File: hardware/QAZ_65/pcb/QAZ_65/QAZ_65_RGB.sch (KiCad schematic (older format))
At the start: 45 parts, among them U3 IS31FL3746A

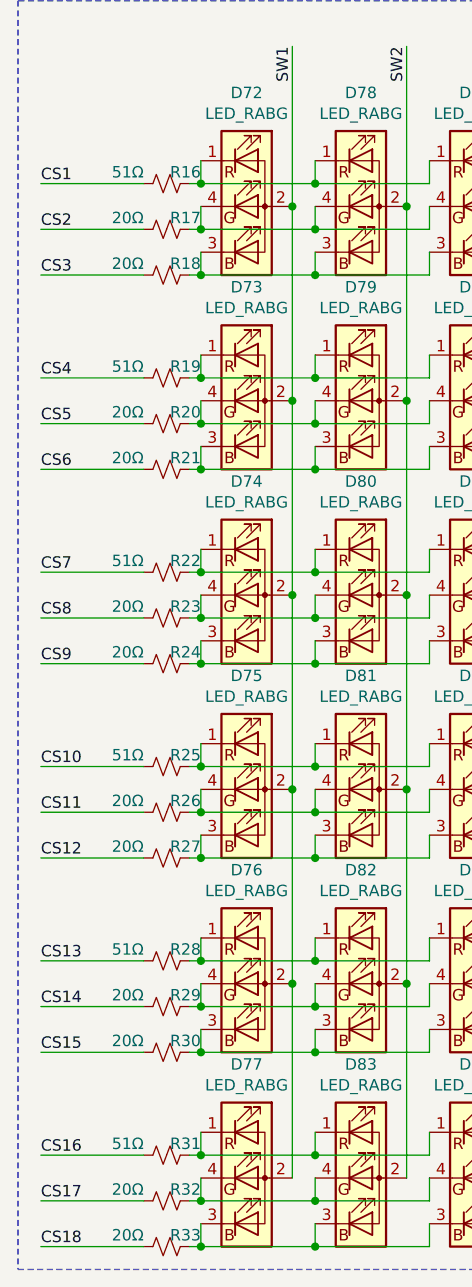
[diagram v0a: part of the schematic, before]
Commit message: layers: added v2/v3 layers for qaz 65%
closes #4

v2 has slightly altered holes on the top of the outline, since the SWD
connector is not brought out.

v3 is for using a pcb as the plate layer (not sure if it will work..)
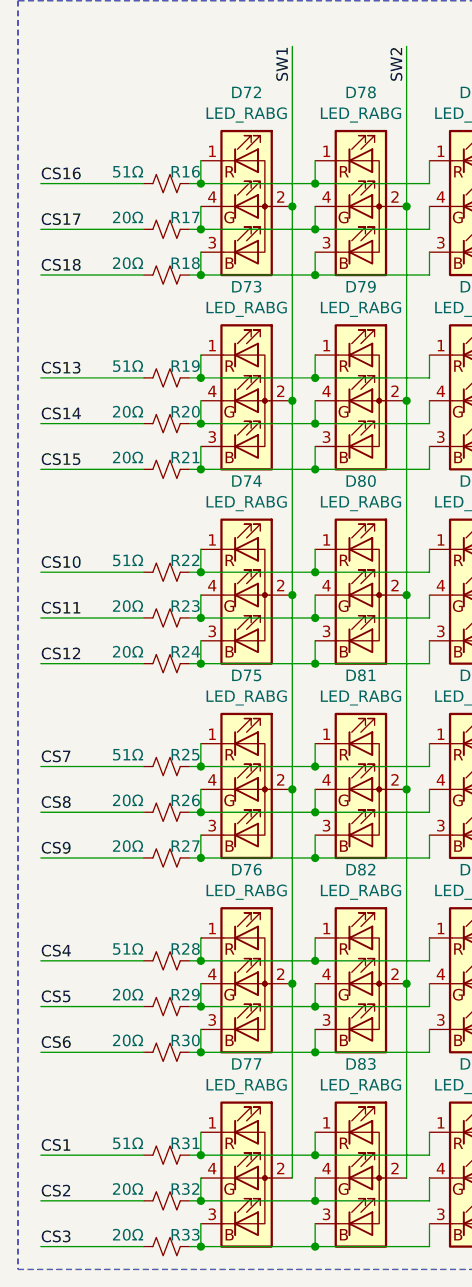
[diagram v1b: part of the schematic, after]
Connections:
- net CS1: now also R31.2; no longer R16.2
- net CS10: now also R22.2; no longer R25.2
- net CS11: now also R23.2; no longer R26.2
- net CS12: now also R24.2; no longer R27.2
- net CS13: now also R19.2; no longer R28.2
- net CS14: now also R20.2; no longer R29.2
- net CS15: now also R21.2; no longer R30.2
- net CS16: now also R16.2; no longer R31.2
- net CS17: now also R17.2; no longer R32.2
- net CS18: now also R18.2; no longer R33.2
- net CS2: now also R32.2; no longer R17.2
- net CS3: now also R33.2; no longer R18.2
- net CS4: now also R28.2; no longer R19.2
- net CS5: now also R29.2; no longer R20.2
- net CS6: now also R30.2; no longer R21.2
- net CS7: now also R25.2; no longer R22.2
- net CS8: now also R26.2; no longer R23.2
- net CS9: now also R27.2; no longer R24.2
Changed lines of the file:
@@
 Wire Wire Line
 	2950 2550 2900 2550
-Text Label 2250 2550 0    50   ~ 0
+Text Label 2250 6800 0    50   ~ 0
 CS3
 Wire Wire Line
-	2700 2550 2250 2550
-Text Label 2250 2350 0    50   ~ 0
+	2700 6800 2250 6800
+Text Label 2250 6600 0    50   ~ 0
 CS2
 Wire Wire Line
-	2700 2350 2250 2350
-Text Label 2250 2150 0    50   ~ 0
+	2700 6600 2250 6600
+Text Label 2250 6400 0    50   ~ 0
 CS1
 Wire Wire Line
-	2700 2150 2250 2150
+	2700 6400 2250 6400
 Wire Wire Line
 	2950 2050 2950 2150
@@
 Wire Wire Line
 	2950 3400 2900 3400
-Text Label 2250 3400 0    50   ~ 0
+Text Label 2250 5950 0    50   ~ 0
 CS6
 Wire Wire Line
-	2700 3400 2250 3400
-Text Label 2250 3200 0    50   ~ 0
+	2700 5950 2250 5950
+Text Label 2250 5750 0    50   ~ 0
 CS5
 Wire Wire Line
-	2700 3200 2250 3200
-Text Label 2250 3000 0    50   ~ 0
+	2700 5750 2250 5750
+Text Label 2250 5550 0    50   ~ 0
 CS4
 Wire Wire Line
-	2700 3000 2250 3000
+	2700 5550 2250 5550
 Wire Wire Line
 	2950 2900 2950 3000
@@
 Wire Wire Line
 	2950 4250 2900 4250
-Text Label 2250 4250 0    50   ~ 0
+Text Label 2250 5100 0    50   ~ 0
 CS9
 Wire Wire Line
-	2700 4250 2250 4250
-Text Label 2250 4050 0    50   ~ 0
+	2700 5100 2250 5100
+Text Label 2250 4900 0    50   ~ 0
 CS8
 Wire Wire Line
-	2700 4050 2250 4050
-Text Label 2250 3850 0    50   ~ 0
+	2700 4900 2250 4900
+Text Label 2250 4700 0    50   ~ 0
 CS7
 Wire Wire Line
-	2700 3850 2250 3850
+	2700 4700 2250 4700
 Wire Wire Line
 	2950 3750 2950 3850
@@
 Wire Wire Line
 	2950 5100 2900 5100
-Text Label 2250 5100 0    50   ~ 0
+Text Label 2250 4250 0    50   ~ 0
 CS12
 Wire Wire Line
-	2700 5100 2250 5100
-Text Label 2250 4900 0    50   ~ 0
+	2700 4250 2250 4250
+Text Label 2250 4050 0    50   ~ 0
 CS11
 Wire Wire Line
-	2700 4900 2250 4900
-Text Label 2250 4700 0    50   ~ 0
+	2700 4050 2250 4050
+Text Label 2250 3850 0    50   ~ 0
 CS10
 Wire Wire Line
-	2700 4700 2250 4700
+	2700 3850 2250 3850
 Wire Wire Line
 	2950 4600 2950 4700
@@
 Wire Wire Line
 	2950 5950 2900 5950
-Text Label 2250 5950 0    50   ~ 0
+Text Label 2250 3400 0    50   ~ 0
 CS15
 Wire Wire Line
-	2700 5950 2250 5950
-Text Label 2250 5750 0    50   ~ 0
+	2700 3400 2250 3400
+Text Label 2250 3200 0    50   ~ 0
 CS14
 Wire Wire Line
-	2700 5750 2250 5750
-Text Label 2250 5550 0    50   ~ 0
+	2700 3200 2250 3200
+Text Label 2250 3000 0    50   ~ 0
 CS13
 Wire Wire Line
-	2700 5550 2250 5550
+	2700 3000 2250 3000
 Wire Wire Line
 	2950 5450 2950 5550
@@
 Wire Wire Line
 	2950 6800 2900 6800
-Text Label 2250 6800 0    50   ~ 0
+Text Label 2250 2550 0    50   ~ 0
 CS18
 Wire Wire Line
-	2700 6800 2250 6800
-Text Label 2250 6600 0    50   ~ 0
+	2700 2550 2250 2550
+Text Label 2250 2350 0    50   ~ 0
 CS17
 Wire Wire Line
-	2700 6600 2250 6600
-Text Label 2250 6400 0    50   ~ 0
+	2700 2350 2250 2350
+Text Label 2250 2150 0    50   ~ 0
 CS16
 Wire Wire Line
-	2700 6400 2250 6400
+	2700 2150 2250 2150
 Wire Wire Line
 	2950 6300 2950 6400

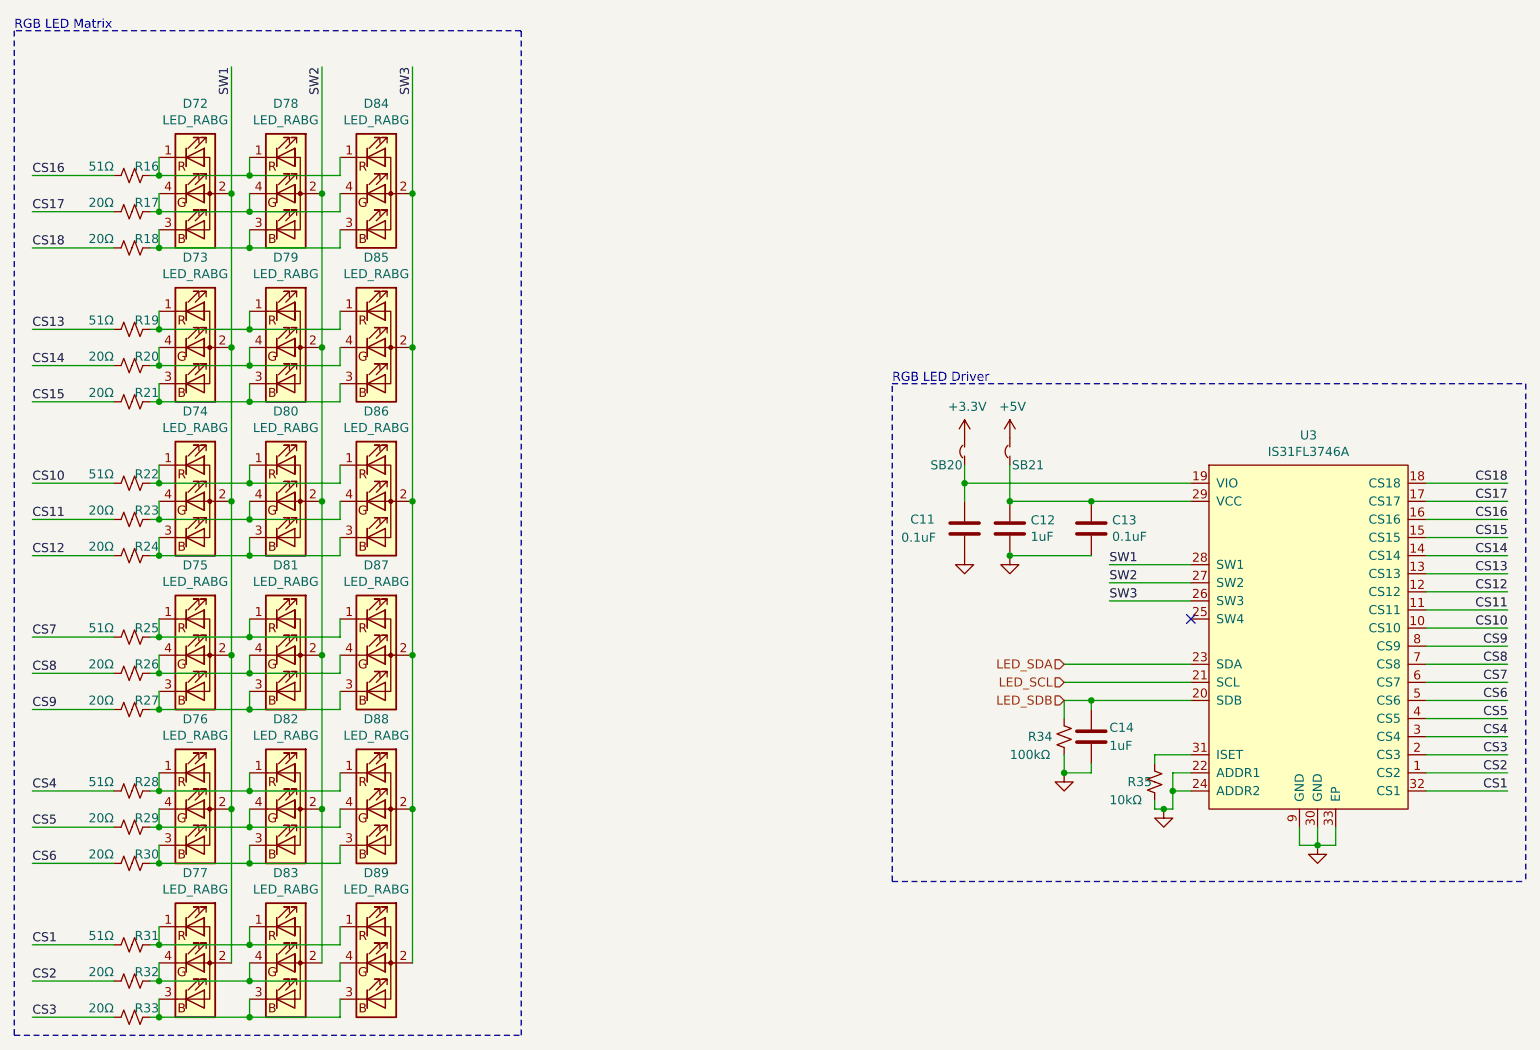
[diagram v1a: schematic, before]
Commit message: breakout: rgb conversion board
Made a conversion board for the LED driver conversion board. The RGB
LEDs chosen will not fit, and must be replaced in QAZ v1.1.
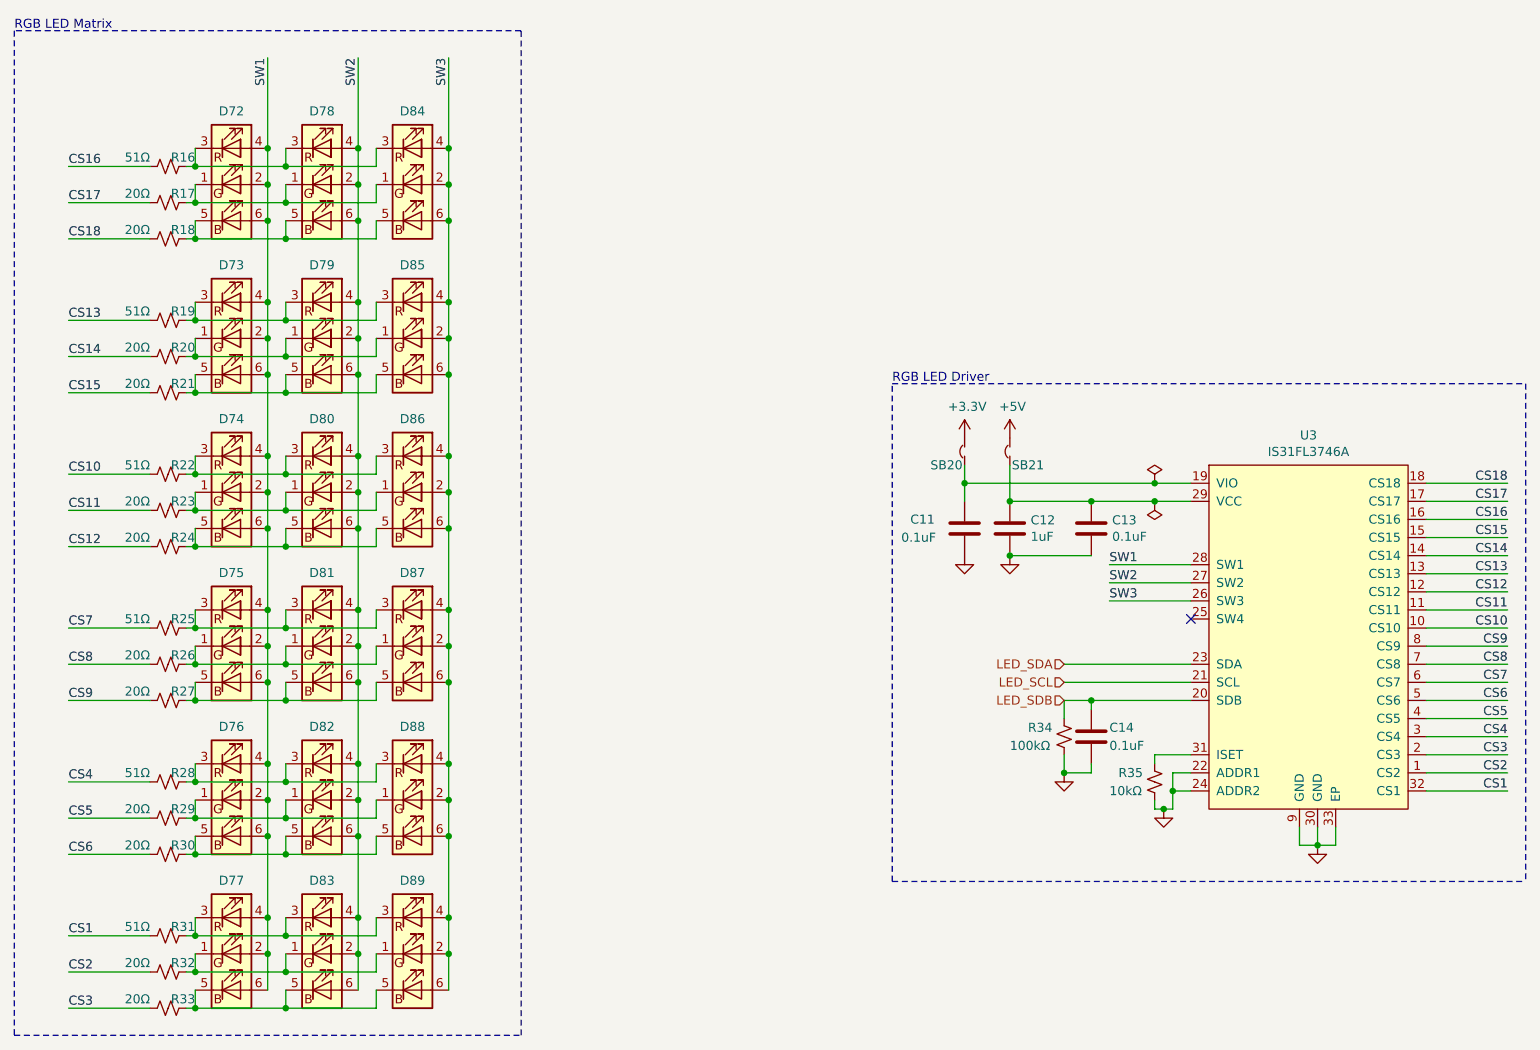
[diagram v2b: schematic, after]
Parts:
- removed D72, D73, D74, D75, D76, D77, D78, D79, D80, D81, D82, D83, D84, D85, D86, D87, D88, D89: LED_RABG, LED_THT:LED_D5.0mm-4_RGB, symbol Device:LED_RABG
- added D72, D73, D74, D75, D76, D77, D78, D79, D80, D81, D82, D83, D84, D85, D86, D87, D88, D89: 19-337C_RSBHGHC-A88_4T, QAZ:0606_1616Metric_HS, symbol QAZ:19-337C_RSBHGHC-A88_4T
- C14: value 1uF -> 0.1uF
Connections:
- net SW1: now also D72.2, D72.4, D72.6, D73.2, D73.4, D73.6, D74.2, D74.4, D74.6, D75.2, D75.4, D75.6, D76.2, D76.4, D76.6, D77.2, D77.4, D77.6
- net SW2: now also D78.2, D78.4, D78.6, D79.2, D79.4, D79.6, D80.2, D80.4, D80.6, D81.2, D81.4, D81.6, D82.2, D82.4, D82.6, D83.2, D83.4, D83.6
- net SW3: now also D84.2, D84.4, D84.6, D85.2, D85.4, D85.6, D86.2, D86.4, D86.6, D87.2, D87.4, D87.6, D88.2, D88.4, D88.6, D89.2, D89.4, D89.6
- net at R16.1: now also D72.3, D78.3, D84.3
- net at R18.1: now also D72.5, D78.5, D84.5
- net at R17.1: now also D72.1, D78.1, D84.1
- net at R19.1: now also D73.3, D79.3, D85.3
- net at R21.1: now also D73.5, D79.5, D85.5
- net at R20.1: now also D73.1, D79.1, D85.1
- net at R22.1: now also D74.3, D80.3, D86.3
- net at R24.1: now also D74.5, D80.5, D86.5
- net at R23.1: now also D74.1, D80.1, D86.1
- net at R25.1: now also D75.3, D81.3, D87.3
- net at R27.1: now also D75.5, D81.5, D87.5
- net at R26.1: now also D75.1, D81.1, D87.1
- net at R28.1: now also D76.3, D82.3, D88.3
- net at R30.1: now also D76.5, D82.5, D88.5
- net at R29.1: now also D76.1, D82.1, D88.1
- net at R31.1: now also D77.3, D83.3, D89.3
- net at R33.1: now also D77.5, D83.5, D89.5
- net at R32.1: now also D77.1, D83.1, D89.1
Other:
- moved on the sheet: R16, R17, R18, R19, R20, R21, R22, R23, R24, R25, R26, R27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
